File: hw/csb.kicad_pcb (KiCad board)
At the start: 2 copper layers, 100 x 90 mm, 55 parts, among them J101 AMPSEAL_23_POS_VERT_BLUE_SEAL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, J102 AMPSEAL_8_POS_VERT_BLACK_SEAL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, J301 ARM_JTAG_SWD_HEADER_10_PINSMD, U301 LPC1549JBD64, U302 MCP2551_SOIC8, U401 VND5050AJTR-E, U501 VN5E010AH, U601 VN5E010AH, U701 VN5E010AH, U901 VND5050AJTR-E, X301 XTAL_7A-12.000MAAJ-T

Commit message: making modifications to pcb...
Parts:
- removed R901, R902: 390, yageo:0603
- added D401: DIODE_RS07J-GS18, usevolt:DO219AB, F.Cu at (175.2, 109.2)
- added D402: DIODE_RS07J-GS18, usevolt:DO219AB, F.Cu at (160.9, 110.5)
- added D501: DIODE_RS07J-GS18, usevolt:DO219AB, F.Cu at (149.5, 83.8)
- added D601: DIODE_RS07J-GS18, usevolt:DO219AB, F.Cu at (157.1, 83.8)
- added D701: DIODE_RS07J-GS18, usevolt:DO219AB, F.Cu at (209.3, 39.9)
- added D801: DIODE_RS07J-GS18, usevolt:DO219AB, F.Cu at (150.3, 39.9)
- added D802: DIODE_RS07J-GS18, usevolt:DO219AB, F.Cu at (150.3, 45.4)
- added R801: 1K, yageo:0603, F.Cu at (172.1, 104.5)
- added R802: 1K, yageo:0603, F.Cu at (173.7, 104.5)
- added U702: VN5E010AH, usevolt:HPAK, F.Cu at (187.1, 98.0)
- R401, R402, R502, R602, R702: value 390 -> 1K
- moved R401 1.00 mm to (165.7, 104.5)
- moved R402 1.00 mm to (167.2, 104.5)
- moved R403 1.00 mm to (164.1, 104.5)
- moved R404 1.00 mm to (162.4, 104.5)
- moved R903 1.00 mm to (170.4, 104.5)
- moved R904 1.00 mm to (168.8, 104.5)
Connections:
- R903 pad 2: /LPC1549/IN -> /Sheet5A02A41E/IN1
- R904 pad 2: /Sheet5A02A41E/IN2 -> /LPC1549/IN
- U301 pad P$1: /Sheet5A02A41E/SENSE2 -> /LPC1549/IN_SENSE
- U301 pad P$2: /LPC1549/IN_SENSE -> /Sheet5A02A41E/SENSE1
- U301 pad P$3: /LPC1549/IN -> /Sheet5A02A41E/IN1
- U301 pad P$4: /Sheet5A02A41E/IN2 -> /LPC1549/IN
- U701 pad 5: /LPC1549/COOLER_SENSE -> (no net)
- U901 pad 2: /Sheet5A02A41E/IN2 -> /LPC1549/IN
- U901 pad 3: /LPC1549/IN -> /Sheet5A02A41E/IN1
- U901 pad 4: /LPC1549/IN_SENSE -> /Sheet5A02A41E/SENSE1
- U901 pad 5: /Sheet5A02A41E/SENSE2 -> /LPC1549/IN_SENSE
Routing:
- net /Sheet5A02A41E/SENSE2: track 78.0 -> 0.00 mm, vias 2 -> 0
- net /Sheet5A02A41E/SENSE1: track 0.00 -> 75.9 mm, vias 0 -> 2
- net /Sheet5A02A41E/IN1: track 0.00 -> 72.8 mm, vias 0 -> 2
- net /Sheet5A02A41E/IN2: track 69.7 -> 0.00 mm, vias 2 -> 0
- net /LPC1549/COOLER: track 70.5 -> 80.8 mm, vias 2 -> 3
- net /LPC1549/COOLER_SENSE: track 70.5 -> 80.7 mm, vias 2 -> 3
- net /LPC1549/IN_SENSE: track 75.0 -> 78.2 mm
- net GND: track 1021.5 -> 1019.0 mm, vias 99 -> 101
- net /LPC1549/BEACON: track 59.7 -> 61.4 mm
- net /LPC1549/BACK: track 61.9 -> 63.1 mm
- net /LPC1549/BACK_SENSE: track 64.1 -> 65.1 mm
- net /LPC1549/IN: track 71.8 -> 71.0 mm
- net /LPC1549/BEACON_SENSE: track 67.2 -> 67.9 mm

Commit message: Drawing pcb 4.0.0
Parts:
- removed D401, D402, D501, D601, D701, D801, D802: DIODE_RS07J-GS18, usevolt:DO219AB
- added D1: ZENER_MM3Z3V6T1G, usevolt:SOD-323, B.Cu at (162.3, 106.5)
- added D2: ZENER_MM3Z3V6T1G, usevolt:SOD-323, B.Cu at (165.6, 106.5)
- added D3: ZENER_MM3Z3V6T1G, usevolt:SOD-323, B.Cu at (147.9, 87.1)
- added D4: ZENER_MM3Z3V6T1G, usevolt:SOD-323, B.Cu at (155.2, 87.1)
- added D5: ZENER_MM3Z3V6T1G, usevolt:SOD-323, B.Cu at (184.8, 86.9)
- added D6: ZENER_MM3Z3V6T1G, usevolt:SOD-323, B.Cu at (173.7, 106.5)
- added D7: ZENER_MM3Z3V6T1G, usevolt:SOD-323, B.Cu at (176.9, 106.5)
- added R1: 10K, yageo:0603, B.Cu at (153.0, 87.0)
- added R2: 10K, yageo:0603, B.Cu at (160.3, 87.0)
- added R3: 10K, yageo:0603, B.Cu at (189.8, 86.9)
- R401, R402, R403, R404, R501, R502, R601, R602, R701, R702, R801, R802, R903, R904: moved to B.Cu
- moved R304 86.8 mm to (141.6, 137.1), turned to 180 degrees
- moved R303 85.8 mm to (138.2, 137.1), turned to 0 degrees
- moved X301 80.3 mm to (131.7, 132.8), turned to 270 degrees
- moved C308 79.1 mm to (134.4, 134.6), turned to 90 degrees
- moved J301 77.7 mm to (139.9, 132.8), turned to 180 degrees
- moved C307 75.7 mm to (134.4, 131.1), turned to 270 degrees
- moved C304 70.4 mm to (138.4, 127.8), turned to 270 degrees
- moved C303 61.6 mm to (148.8, 121.4), turned to 0 degrees
- moved D202 57.3 mm to (200.2, 123.3), turned to 180 degrees
- moved C302 57.2 mm to (148.9, 118.8), turned to 0 degrees
- moved F201 53.8 mm to (200.7, 119.4), turned to 180 degrees
- moved D201 51.6 mm to (200.5, 116.8), turned to 0 degrees
- moved C202 51.5 mm to (191.2, 132.7), turned to 180 degrees
- moved U301 51.3 mm to (140.2, 119.1), turned to 180 degrees
- moved C306 47.9 mm to (131.4, 117.8), turned to 180 degrees
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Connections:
- J101 pad P$12: (no net) -> Net-(J101-PadP$12)
- J101 pad P$14: (no net) -> Net-(J101-PadP$14)
- J101 pad P$4: (no net) -> Net-(J101-PadP$4)
- J101 pad P$5: (no net) -> Net-(J101-PadP$5)
- J101 pad P$6: (no net) -> Net-(J101-PadP$6)
- J101 pad P$7: (no net) -> Net-(J101-PadP$7)
- J102 pad P$7: (no net) -> Net-(J102-PadP$7)
- J102 pad P$8: (no net) -> Net-(J102-PadP$8)
- J301 pad P$6: (no net) -> Net-(J301-PadP$6)
- J301 pad P$7: (no net) -> Net-(J301-PadP$7)
- J301 pad P$8: (no net) -> Net-(J301-PadP$8)
- U301 pad P$15: (no net) -> Net-(U301-PadP$15)
- U301 pad P$16: (no net) -> Net-(U301-PadP$16)
- U301 pad P$17: (no net) -> Net-(U301-PadP$17)
- U301 pad P$19: (no net) -> Net-(U301-PadP$19)
- U301 pad P$23: (no net) -> Net-(U301-PadP$23)
- U301 pad P$24: (no net) -> Net-(U301-PadP$24)
- U301 pad P$25: (no net) -> Net-(U301-PadP$25)
- U301 pad P$28: (no net) -> Net-(U301-PadP$28)
- U301 pad P$31: (no net) -> Net-(U301-PadP$31)
- U301 pad P$32: (no net) -> Net-(U301-PadP$32)
- U301 pad P$38: (no net) -> Net-(U301-PadP$38)
- U301 pad P$39: (no net) -> Net-(U301-PadP$39)
- U301 pad P$42: (no net) -> Net-(U301-PadP$42)
- U301 pad P$43: (no net) -> Net-(U301-PadP$43)
- U301 pad P$46: (no net) -> Net-(U301-PadP$46)
- U301 pad P$47: (no net) -> Net-(U301-PadP$47)
- U301 pad P$48: (no net) -> Net-(U301-PadP$48)
- U301 pad P$49: (no net) -> Net-(U301-PadP$49)
- U301 pad P$50: (no net) -> Net-(U301-PadP$50)
- U301 pad P$51: (no net) -> Net-(U301-PadP$51)
- U301 pad P$53: (no net) -> Net-(U301-PadP$53)
- U301 pad P$54: (no net) -> Net-(U301-PadP$54)
- U301 pad P$58: (no net) -> Net-(U301-PadP$58)
- U301 pad P$61: (no net) -> Net-(U301-PadP$61)
- U301 pad P$62: (no net) -> Net-(U301-PadP$62)
- U301 pad P$63: (no net) -> Net-(U301-PadP$63)
- U301 pad P$64: (no net) -> Net-(U301-PadP$64)
- U302 pad 5: (no net) -> Net-(U302-Pad5)
- U401 pad 6: (no net) -> Net-(U401-Pad6)
- U701 pad 5: (no net) -> Net-(U701-Pad5)
- U901 pad 6: (no net) -> Net-(U901-Pad6)
- VR201 pad 2: (no net) -> Net-(VR201-Pad2)
- VR201 pad 3: (no net) -> Net-(VR201-Pad3)
- VR201 pad 5: (no net) -> Net-(VR201-Pad5)
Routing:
- net GND: track 1019.0 -> 0.00 mm, vias 101 -> 0
- net +3V3: track 143.6 -> 0.00 mm
- net /LPC1549/COOLER: track 80.8 -> 0.00 mm, vias 3 -> 0
- net /LPC1549/COOLER_SENSE: track 80.7 -> 0.00 mm, vias 3 -> 0
- net /LPC1549/IN_SENSE: track 78.2 -> 0.00 mm, vias 2 -> 0
- net /Sheet5A02A41E/SENSE1: track 75.9 -> 0.00 mm, vias 2 -> 0
- net /Sheet5A02A41E/IN1: track 72.8 -> 0.00 mm, vias 2 -> 0
- net /LPC1549/IN: track 71.0 -> 0.00 mm, vias 2 -> 0
- net /LPC1549/BEACON_SENSE: track 67.9 -> 0.00 mm, vias 2 -> 0
- net /LPC1549/BACK_SENSE: track 65.1 -> 0.00 mm, vias 2 -> 0
- net /LPC1549/BACK: track 63.1 -> 0.00 mm, vias 2 -> 0
- net /LPC1549/BEACON: track 61.4 -> 0.00 mm, vias 2 -> 0
- net /LPC1549/CAN_RX: track 56.9 -> 0.00 mm
- net /LPC1549/CAN_TX: track 52.1 -> 0.00 mm
- net /Sheet5A019745/IN1: track 46.8 -> 0.00 mm, vias 2 -> 0
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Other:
- board size 100 x 90 mm -> 78 x 90 mm

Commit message: pcb 3.4.0 created, ready for order
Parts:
- D1, D2, D6, D7, R401, R402, R403, R404, R801, R802, R903, R904: moved to F.Cu
- moved D1 7.95 mm to (162.2, 98.5)
- moved D2 7.95 mm to (165.3, 98.5)
- moved D6 7.95 mm to (173.5, 98.5)
- moved D7 7.95 mm to (176.7, 98.5)
- moved R401 7.95 mm to (163.8, 98.5)
- moved R402 7.95 mm to (166.9, 98.5)
- moved R403 7.95 mm to (160.6, 98.5)
- moved R404 7.95 mm to (158.8, 98.5)
- moved R801 7.95 mm to (171.9, 98.5)
- moved R802 7.95 mm to (175.1, 98.5)
- moved R903 7.95 mm to (170.2, 98.5)
- moved R904 7.95 mm to (168.6, 98.5)
- moved D3 5.50 mm to (147.9, 81.6)
- moved D4 5.50 mm to (155.2, 81.6)
- moved D5 5.50 mm to (184.8, 81.4)
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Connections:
- U301 pad P$15: Net-(U301-PadP$15) -> Net-(R301-Pad2)
- U301 pad P$16: Net-(U301-PadP$16) -> Net-(R302-Pad2)
- U301 pad P$33: Net-(R301-Pad2) -> Net-(U301-PadP$33)
- U301 pad P$34: Net-(R302-Pad2) -> Net-(U301-PadP$34)
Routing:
- net /LPC1549/COOLER: track 0.00 -> 91.0 mm, vias 0 -> 3
- net /LPC1549/COOLER_SENSE: track 0.00 -> 78.8 mm, vias 0 -> 2
- net +3V3: track 0.00 -> 70.9 mm
- net GND: track 0.00 -> 67.5 mm, vias 0 -> 92
- net Net-(R302-Pad2): track 0.00 -> 52.1 mm
- net Net-(R301-Pad2): track 0.00 -> 50.5 mm
- net /LPC1549/IN_SENSE: track 0.00 -> 46.4 mm, vias 0 -> 2
- net /LPC1549/COOLER_P: track 0.00 -> 45.8 mm
- net /Sheet5A02A41E/SENSE1: track 0.00 -> 43.2 mm, vias 0 -> 2
- net /Sheet5A019745/SENSE1: track 0.00 -> 42.9 mm, vias 0 -> 2
- net /Sheet5A019745/IN1: track 0.00 -> 41.3 mm, vias 0 -> 2
- net /LPC1549/IN: track 0.00 -> 40.0 mm, vias 0 -> 2
- net /Sheet5A02A41E/IN1: track 0.00 -> 39.4 mm, vias 0 -> 2
- net /LPC1549/DRIVE_SENSE: track 0.00 -> 38.5 mm, vias 0 -> 2
- net +5V: track 0.00 -> 38.3 mm
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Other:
- board text added: "Usewood CSB Usevolt Oy 3.4.0"
- board text removed: "Usewood CSB Usevolt Oy"

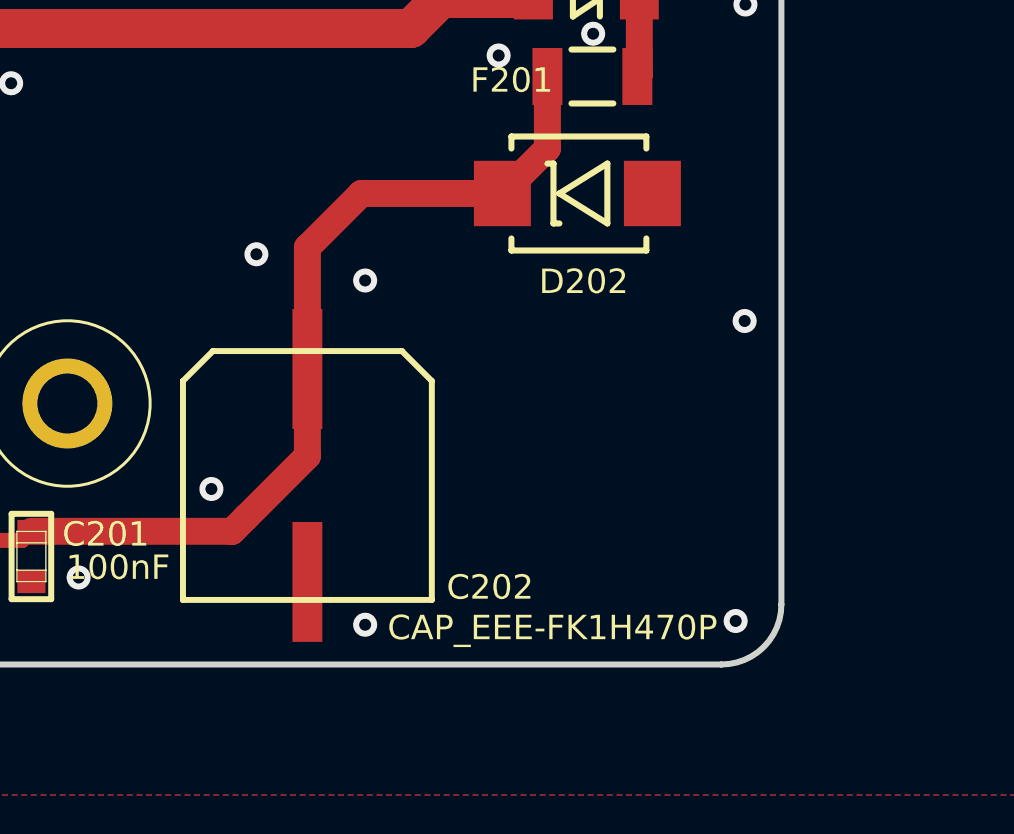
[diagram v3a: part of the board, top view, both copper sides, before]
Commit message: CAP moved away from AMPSEAL leg
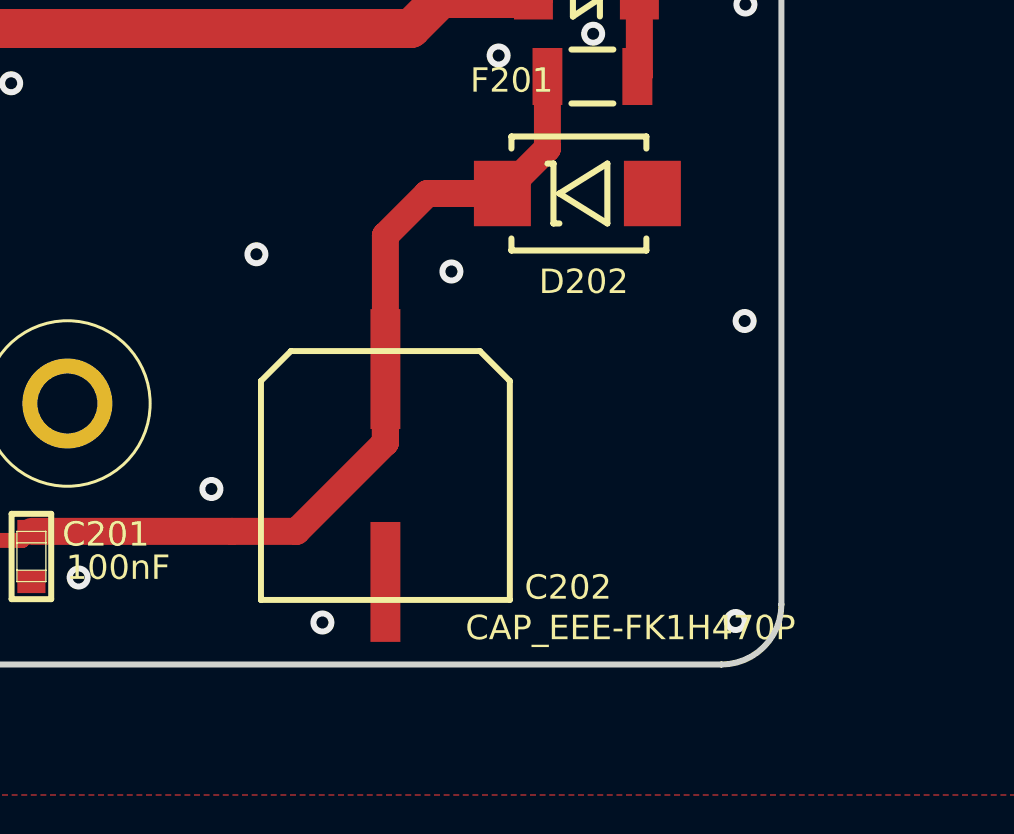
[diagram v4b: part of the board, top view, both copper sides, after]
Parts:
- moved C202 2.60 mm to (193.8, 132.7)
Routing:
- net Net-(C201-Pad1): track 31.3 -> 33.7 mm
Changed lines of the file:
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@@
     (thickness 1.6)
     (drawings 9)
-    (tracks 678)
+    (tracks 677)
     (zones 0)
     (modules 66)
@@
   )
   (setup
-    (last_trace_width 0.2)
+    (last_trace_width 0.9)
     (user_trace_width 0.3)
     (user_trace_width 0.5)
@@
   )
   (module usevolt:CAP_EEE-FK1H470P (layer F.Cu)
-    (at 191.2 132.7 180)
+    (at 193.8 132.7 180)
     (attr smd)
     (fp_text reference C202 (at -6.09 -3.73 180) (layer F.SilkS)
@@
     (effects (font (size 1.5 1.5) (thickness 0.3)))
   )
+  (via (at 196 125.9) (size 0.8) (drill 0.4) (layers F.Cu B.Cu) (net 1))
+  (via (at 191.7 137.6) (size 0.8) (drill 0.4) (layers F.Cu B.Cu) (net 1))
   (via (at 133.05 138.01) (size 0.8) (drill 0.4) (layers F.Cu B.Cu) (net 1))
   (via (at 152.31 133.63) (size 0.8) (drill 0.4) (layers F.Cu B.Cu) (net 1))
@@
   (via (at 205.775 127.55) (size 0.8) (drill 0.4) (layers F.Cu B.Cu) (net 1))
   (via (at 205.475 137.55) (size 0.8) (drill 0.4) (layers F.Cu B.Cu) (net 1))
-  (via (at 193.125 137.675) (size 0.8) (drill 0.4) (layers F.Cu B.Cu) (net 1))
-  (via (at 193.125 126.2) (size 0.8) (drill 0.4) (layers F.Cu B.Cu) (net 1))
   (via (at 189.5 125.325) (size 0.8) (drill 0.4) (layers F.Cu B.Cu) (net 1))
   (via (at 200.725 117.975) (size 0.8) (drill 0.4) (layers F.Cu B.Cu) (net 1))
@@
   (segment (start 171.1 88.6) (end 171.55 88.15) (width 0.4) (layer F.Cu) (net 18))
   (segment (start 171.1 89.6) (end 171.1 88.6) (width 0.4) (layer F.Cu) (net 18))
+  (segment (start 193.8 129.15162) (end 193.8 131.6) (width 0.9) (layer F.Cu) (net 19))
+  (segment (start 195.2 123.3) (end 193.8 124.7) (width 0.9) (layer F.Cu) (net 19))
+  (segment (start 197.7 123.3) (end 195.2 123.3) (width 0.9) (layer F.Cu) (net 19))
+  (segment (start 193.8 124.7) (end 193.8 131.6) (width 0.9) (layer F.Cu) (net 19))
+  (segment (start 190.8382 134.5618) (end 188.6882 134.5618) (width 0.9) (layer F.Cu) (net 19))
+  (segment (start 193.8 131.6) (end 190.8382 134.5618) (width 0.9) (layer F.Cu) (net 19))
+  (segment (start 188.6882 134.5618) (end 182 134.5618) (width 0.9) (layer F.Cu) (net 19))
   (segment (start 179.821 134.865) (end 181.6968 134.865) (width 0.5) (layer F.Cu) (net 19))
   (segment (start 181.6968 134.865) (end 182 134.5618) (width 0.5) (layer F.Cu) (net 19))
-  (segment (start 191.2 132.0506) (end 189.1506 134.1) (width 0.9) (layer F.Cu) (net 19))
-  (segment (start 191.2 129.15162) (end 191.2 132.0506) (width 0.9) (layer F.Cu) (net 19))
-  (segment (start 189.1506 134.1) (end 189.15 134.1) (width 0.9) (layer F.Cu) (net 19))
-  (segment (start 189.15 134.1) (end 188.6882 134.5618) (width 0.9) (layer F.Cu) (net 19))
-  (segment (start 188.6882 134.5618) (end 182 134.5618) (width 0.9) (layer F.Cu) (net 19))
-  (segment (start 193 123.3) (end 191.2 125.1) (width 0.9) (layer F.Cu) (net 19))
-  (segment (start 191.2 125.1) (end 191.2 129.15162) (width 0.9) (layer F.Cu) (net 19))
-  (segment (start 197.7 123.3) (end 193 123.3) (width 0.9) (layer F.Cu) (net 19))
   (segment (start 199.2014 119.4) (end 199.2014 121.7986) (width 0.9) (layer F.Cu) (net 19))
   (segment (start 199.2014 121.7986) (end 197.7 123.3) (width 0.9) (layer F.Cu) (net 19))
